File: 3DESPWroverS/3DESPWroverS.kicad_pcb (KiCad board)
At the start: 2 copper layers, 44.5 x 44.5 mm, 9 parts, among them J1 Conn_02x03_Odd_Even, J2 Conn_01x01, J3 Conn_01x01, J4 Conn_01x01, J5 Conn_01x01, J6 Conn_01x01, J7 Conn_01x01, J8 Conn_01x01, J9 Conn_01x01

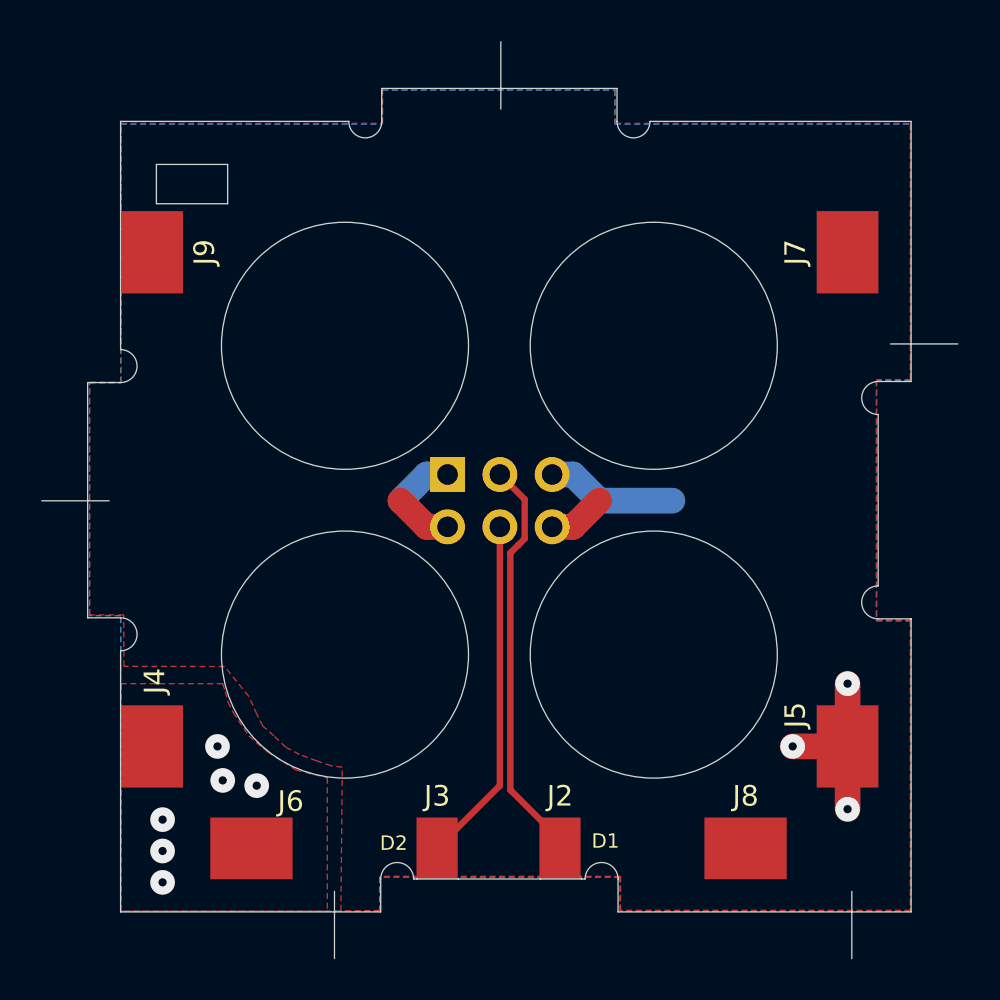
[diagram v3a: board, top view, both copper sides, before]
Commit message: Added 0805 diode before 3.3 power source
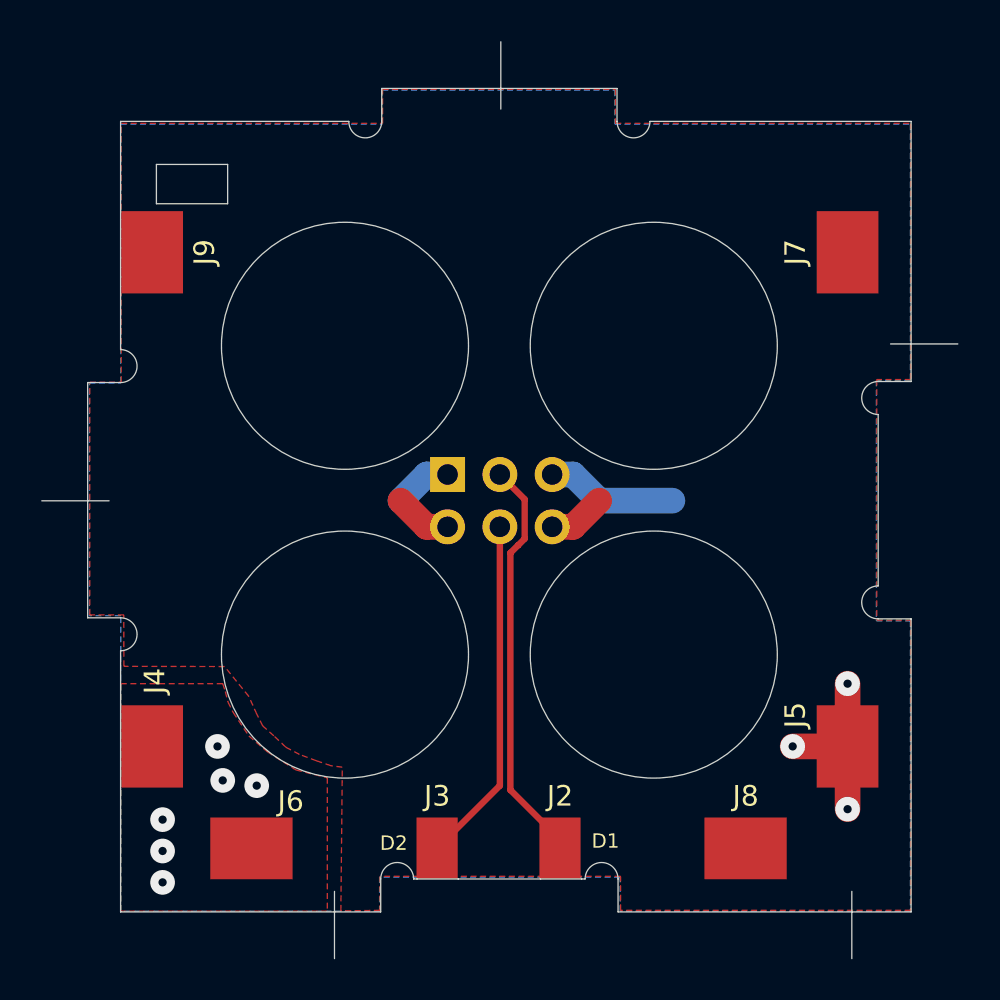
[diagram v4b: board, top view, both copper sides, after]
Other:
- net class Default removed
- net class Power removed
